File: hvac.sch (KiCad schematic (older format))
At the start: 44 parts, among them IC1 ATMEGA328P-A, J1 PROGRAMMING HEADER, J2 SERIAL PORT, J3 POWER_INPUT, M1 PINHD-1X10, SW1 SPST, SW2 SPST, SW3 SPST, U1 MIC5225, U2 MOSFET_N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

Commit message: Begin routing
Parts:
- removed D1, D5: RED, MF_LEDs:MF_LEDs-LED0603, symbol LED
- removed D2: YELLOW, MF_LEDs:MF_LEDs-LED0603, symbol LED
- removed D3: GREEN, MF_LEDs:MF_LEDs-LED0603, symbol LED
- removed D4: BLUE, MF_LEDs:MF_LEDs-LED0603, symbol LED
- removed M1: PINHD-1X10, Air_Coils_SML_NEOSID:Neosid_Air-Coil_SML_1turn_HDM0131A, symbol PINHD-1X10
- added D1, D5: RED, MF_LEDs:MF_LEDs-LED0603, symbol LED_SINGLE-0603-RED
- added D2: YELLOW, MF_LEDs:MF_LEDs-LED0603, symbol LED_SINGLE-0603
- added D3: GREEN, MF_LEDs:MF_LEDs-LED0603, symbol LED_SINGLE-0603-GREEN
- added D4: BLUE, MF_LEDs:MF_LEDs-LED0603, symbol LED_SINGLE-0603
- added JP2: PINHD-1X9, homebrew:1x9-RIGHT_ANGLE-0534260910, symbol PINHD-1X9
- BTN1: footprint (none) -> homebrew:EG2355-ND
- F1: footprint Air_Coils_SML_NEOSID:Neosid_Air-Coil_SML_1turn_HDM0131A -> homebrew:FUSE-3550-2
- J3: footprint Air_Coils_SML_NEOSID:Neosid_Air-Coil_SML_1turn_HDM0131A -> homebrew:1x2-RIGHT_ANGLE-43160-1102
- JP1: footprint Air_Coils_SML_NEOSID:Neosid_Air-Coil_SML_1turn_HDM0131A -> homebrew:1x6-RIGHT_ANGLE-43160-3106
- RV1, RV2: footprint Air_Coils_SML_NEOSID:Neosid_Air-Coil_SML_1turn_HDM0131A -> homebrew:PDB12-H4301-103BF
- SW1, SW2, SW3: footprint Air_Coils_SML_NEOSID:Neosid_Air-Coil_SML_1turn_HDM0131A -> homebrew:EG2355-ND
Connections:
- wire segments 118 -> 102
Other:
- moved on the sheet: R5, R6, R7, R8, R9
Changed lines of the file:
@@
 L RESISTOR0402 R5
 U 1 1 590EB7DD
-P 5450 6800
-F 0 "R5" H 5300 6859 50  0000 L BNN
-F 1 "2.2k" H 5300 6670 50  0000 L BNN
-F 2 "Resistors_SMD:R_0402" H 5480 6950 20  0001 C CNN
-F 3 "" H 5450 6800 60  0000 C CNN
-	1    5450 6800
+P 5450 7100
+F 0 "R5" H 5300 7159 50  0000 L BNN
+F 1 "2.2k" H 5300 6970 50  0000 L BNN
+F 2 "Resistors_SMD:R_0402" H 5480 7250 20  0001 C CNN
+F 3 "" H 5450 7100 60  0000 C CNN
+	1    5450 7100
 	0    1    1    0
 $EndComp
@@
 L RESISTOR0402 R6
 U 1 1 590EB81A
-P 5750 6800
-F 0 "R6" H 5600 6859 50  0000 L BNN
-F 1 "2.2k" H 5600 6670 50  0000 L BNN
-F 2 "Resistors_SMD:R_0402" H 5780 6950 20  0001 C CNN
-F 3 "" H 5750 6800 60  0000 C CNN
-	1    5750 6800
+P 5750 7100
+F 0 "R6" H 5600 7159 50  0000 L BNN
+F 1 "2.2k" H 5600 6970 50  0000 L BNN
+F 2 "Resistors_SMD:R_0402" H 5780 7250 20  0001 C CNN
+F 3 "" H 5750 7100 60  0000 C CNN
+	1    5750 7100
 	0    1    1    0
 $EndComp
@@
 L RESISTOR0402 R7
 U 1 1 590EB84F
-P 6050 6800
-F 0 "R7" H 5900 6859 50  0000 L BNN
-F 1 "2.2k" H 5900 6670 50  0000 L BNN
-F 2 "Resistors_SMD:R_0402" H 6080 6950 20  0001 C CNN
-F 3 "" H 6050 6800 60  0000 C CNN
-	1    6050 6800
-	0    1    1    0
-$EndComp
-$Comp
-L LED D1
-U 1 1 590EB886
-P 5450 7250
-F 0 "D1" H 5450 7350 50  0000 C CNN
-F 1 "RED" H 5450 7150 50  0000 C CNN
-F 2 "MF_LEDs:MF_LEDs-LED0603" H 5450 7250 50  0001 C CNN
-F 3 "" H 5450 7250 50  0000 C CNN
-	1    5450 7250
-	0    -1   -1   0
-$EndComp
-$Comp
-L LED D2
-U 1 1 590EB8BF
-P 5750 7250
-F 0 "D2" H 5750 7350 50  0000 C CNN
-F 1 "YELLOW" H 5750 7150 50  0000 C CNN
-F 2 "MF_LEDs:MF_LEDs-LED0603" H 5750 7250 50  0001 C CNN
-F 3 "" H 5750 7250 50  0000 C CNN
-	1    5750 7250
-	0    -1   -1   0
-$EndComp
-$Comp
-L LED D3
-U 1 1 590EB8F6
-P 6050 7250
-F 0 "D3" H 6050 7350 50  0000 C CNN
-F 1 "GREEN" H 6050 7150 50  0000 C CNN
-F 2 "MF_LEDs:MF_LEDs-LED0603" H 6050 7250 50  0001 C CNN
-F 3 "" H 6050 7250 50  0000 C CNN
-	1    6050 7250
-	0    -1   -1   0
-$EndComp
-Wire Wire Line
-	6050 7000 6050 7050
-Wire Wire Line
-	5750 7050 5750 7000
-Wire Wire Line
-	5450 7000 5450 7050
-Wire Wire Line
-	5450 7450 5450 7500
-Wire Wire Line
-	5750 7500 5750 7450
-Wire Wire Line
-	6050 7450 6050 7500
-Text GLabel 5450 6550 1    60   Input ~ 0
+P 6050 7100
+F 0 "R7" H 5900 7159 50  0000 L BNN
+F 1 "2.2k" H 5900 6970 50  0000 L BNN
+F 2 "Resistors_SMD:R_0402" H 6080 7250 20  0001 C CNN
+F 3 "" H 6050 7100 60  0000 C CNN
+	1    6050 7100
+	0    1    1    0
+$EndComp
+Text GLabel 5450 6900 1    60   Input ~ 0
 LED_R
-Wire Wire Line
-	5450 6550 5450 6600
-Wire Wire Line
-	5750 6600 5750 6550
-Wire Wire Line
-	6050 6550 6050 6600
-Text GLabel 6050 6550 1    60   Input ~ 0
+Text GLabel 6050 6900 1    60   Input ~ 0
 LED_G
-Text GLabel 5750 6550 1    60   Input ~ 0
+Text GLabel 5750 6900 1    60   Input ~ 0
 LED_Y
 Wire Notes Line
@@
 L RESISTOR0402 R8
 U 1 1 590EC9AA
-P 6350 6800
-F 0 "R8" H 6200 6859 50  0000 L BNN
-F 1 "2.2k" H 6200 6670 50  0000 L BNN
-F 2 "Resistors_SMD:R_0402" H 6380 6950 20  0001 C CNN
-F 3 "" H 6350 6800 60  0000 C CNN
-	1    6350 6800
-	0    1    1    0
-$EndComp
-$Comp
-L LED D4
-U 1 1 590EC9B0
-P 6350 7250
-F 0 "D4" H 6350 7350 50  0000 C CNN
-F 1 "BLUE" H 6350 7150 50  0000 C CNN
-F 2 "MF_LEDs:MF_LEDs-LED0603" H 6350 7250 50  0001 C CNN
-F 3 "" H 6350 7250 50  0000 C CNN
-	1    6350 7250
-	0    -1   -1   0
-$EndComp
-Wire Wire Line
-	6350 7000 6350 7050
-Wire Wire Line
-	6350 7450 6350 7500
-Wire Wire Line
-	6350 6550 6350 6600
-Text GLabel 6350 6550 1    60   Input ~ 0
+P 6350 7100
+F 0 "R8" H 6200 7159 50  0000 L BNN
+F 1 "2.2k" H 6200 6970 50  0000 L BNN
+F 2 "Resistors_SMD:R_0402" H 6380 7250 20  0001 C CNN
+F 3 "" H 6350 7100 60  0000 C CNN
+	1    6350 7100
+	0    1    1    0
+$EndComp
+Text GLabel 6350 6900 1    60   Input ~ 0
 LED_TIMER
 $Comp
@@
 F 0 "SW1" H 9500 800 50  0000 C CNN
 F 1 "SPST" H 9500 600 50  0000 C CNN
-F 2 "Air_Coils_SML_NEOSID:Neosid_Air-Coil_SML_1turn_HDM0131A" H 9500 700 50  0001 C CNN
+F 2 "homebrew:EG2355-ND" H 9500 700 50  0001 C CNN
 F 3 "" H 9500 700 50  0000 C CNN
 	1    9500 700
@@
 F 0 "SW2" H 9500 1050 50  0000 C CNN
 F 1 "SPST" H 9500 850 50  0000 C CNN
-F 2 "Air_Coils_SML_NEOSID:Neosid_Air-Coil_SML_1turn_HDM0131A" H 9500 950 50  0001 C CNN
+F 2 "homebrew:EG2355-ND" H 9500 950 50  0001 C CNN
 F 3 "" H 9500 950 50  0000 C CNN
 	1    9500 950
@@
 F 0 "SW3" H 9500 1300 50  0000 C CNN
 F 1 "SPST" H 9500 1100 50  0000 C CNN
-F 2 "Air_Coils_SML_NEOSID:Neosid_Air-Coil_SML_1turn_HDM0131A" H 9500 1200 50  0001 C CNN
+F 2 "homebrew:EG2355-ND" H 9500 1200 50  0001 C CNN
 F 3 "" H 9500 1200 50  0000 C CNN
 	1    9500 1200
@@
 F 0 "RV1" H 9350 1920 50  0000 C CNN
 F 1 "POT" H 9350 2000 50  0000 C CNN
-F 2 "Air_Coils_SML_NEOSID:Neosid_Air-Coil_SML_1turn_HDM0131A" H 9350 2000 50  0001 C CNN
+F 2 "homebrew:PDB12-H4301-103BF" H 9350 2000 50  0001 C CNN
 F 3 "" H 9350 2000 50  0000 C CNN
 	1    9350 2000
@@
 F 0 "RV2" H 9350 2470 50  0000 C CNN
 F 1 "POT" H 9350 2550 50  0000 C CNN
-F 2 "Air_Coils_SML_NEOSID:Neosid_Air-Coil_SML_1turn_HDM0131A" H 9350 2550 50  0001 C CNN
+F 2 "homebrew:PDB12-H4301-103BF" H 9350 2550 50  0001 C CNN
 F 3 "" H 9350 2550 50  0000 C CNN
 	1    9350 2550
@@
 L RESISTOR0402 R9
 U 1 1 590F35DB
-P 6650 6800
-F 0 "R9" H 6500 6859 50  0000 L BNN
-F 1 "2.2k" H 6500 6670 50  0000 L BNN
-F 2 "Resistors_SMD:R_0402" H 6680 6950 20  0001 C CNN
-F 3 "" H 6650 6800 60  0000 C CNN
-	1    6650 6800
-	0    1    1    0
-$EndComp
-$Comp
-L LED D5
-U 1 1 590F35E1
-P 6650 7250
-F 0 "D5" H 6650 7350 50  0000 C CNN
-F 1 "RED" H 6650 7150 50  0000 C CNN
-F 2 "MF_LEDs:MF_LEDs-LED0603" H 6650 7250 50  0001 C CNN
-F 3 "" H 6650 7250 50  0000 C CNN
-	1    6650 7250
-	0    -1   -1   0
-$EndComp
-Wire Wire Line
-	6650 7000 6650 7050
-Wire Wire Line
-	6650 7450 6650 7500
-Wire Wire Line
-	6650 6550 6650 6600
-Text GLabel 6650 6550 1    60   Input ~ 0
+P 6650 7100
+F 0 "R9" H 6500 7159 50  0000 L BNN
+F 1 "2.2k" H 6500 6970 50  0000 L BNN
+F 2 "Resistors_SMD:R_0402" H 6680 7250 20  0001 C CNN
+F 3 "" H 6650 7100 60  0000 C CNN
+	1    6650 7100
+	0    1    1    0
+$EndComp
+Text GLabel 6650 6900 1    60   Input ~ 0
 LED_WATER_LIMIT
 Wire Wire Line
@@
 F 0 "BTN1" H 9500 1550 50  0000 C CNN
 F 1 "SPST" H 9500 1350 50  0001 C CNN
-F 2 "" H 9500 1450 50  0001 C CNN
+F 2 "homebrew:EG2355-ND" H 9500 1450 50  0001 C CNN
 F 3 "" H 9500 1450 50  0000 C CNN
 	1    9500 1450
@@
 F 0 "J3" H 4800 6150 50  0001 C CNN
 F 1 "POWER_INPUT" H 4800 6150 50  0001 C CNN
-F 2 "Air_Coils_SML_NEOSID:Neosid_Air-Coil_SML_1turn_HDM0131A" H 4830 6300 20  0001 C CNN
+F 2 "homebrew:1x2-RIGHT_ANGLE-43160-1102" H 4830 6300 20  0001 C CNN
 F 3 "" H 4800 6150 60  0000 C CNN
 	1    4800 6150
@@
 F 0 "JP1" H 10200 5375 50  0000 L BNN
 F 1 "PINHD-1X6" H 10200 4550 50  0000 L BNN
-F 2 "Air_Coils_SML_NEOSID:Neosid_Air-Coil_SML_1turn_HDM0131A" H 10480 5100 20  0001 C CNN
+F 2 "homebrew:1x6-RIGHT_ANGLE-43160-3106" H 10480 5100 20  0001 C CNN
 F 3 "" H 10450 4950 60  0000 C CNN
 	1    10450 4950
@@
 F 0 "F1" H 3800 6150 50  0000 L BNN
 F 1 "POWER_FUSE" H 4400 6150 50  0000 L BNN
-F 2 "Air_Coils_SML_NEOSID:Neosid_Air-Coil_SML_1turn_HDM0131A" H 4230 6200 20  0001 C CNN
+F 2 "homebrew:FUSE-3550-2" H 4230 6200 20  0001 C CNN
 F 3 "" H 4200 6050 60  0000 C CNN
 	1    4200 6050
@@
 Text Notes 350  6400 0    60   ~ 0
 TODO: Verify programming port
-$Comp
-L PINHD-1X10 M1
-U 1 1 5910F906
-P 10450 3650
-F 0 "M1" H 10200 4175 50  0000 L BNN
-F 1 "PINHD-1X10" H 10200 2950 50  0000 L BNN
-F 2 "Air_Coils_SML_NEOSID:Neosid_Air-Coil_SML_1turn_HDM0131A" H 10480 3800 20  0001 C CNN
-F 3 "" H 10450 3650 60  0000 C CNN
-	1    10450 3650
-	1    0    0    -1
-$EndComp
 Wire Wire Line
 	9150 3200 9150 3650
@@
 	10350 3950 9250 3950
 Connection ~ 9250 3950
-Wire Wire Line
-	9250 4150 10350 4150
 Connection ~ 9250 4150
 Wire Wire Line
@@
 	800  1600 800  1800
 Wire Wire Line
-	800  1300 800  1150
+	800  1150 800  1300
 Wire Wire Line
 	1950 1500 1950 1800
@@
 Wire Wire Line
 	1200 1500 1950 1500
+$Comp
+L PINHD-1X9 JP2
+U 1 1 591172FD
+P 10450 3650
+F 0 "JP2" H 10200 4175 50  0000 L BNN
+F 1 "PINHD-1X9" H 10200 3050 50  0000 L BNN
+F 2 "homebrew:1x9-RIGHT_ANGLE-0534260910" H 10480 3800 20  0001 C CNN
+F 3 "" H 10450 3650 60  0000 C CNN
+	1    10450 3650
+	1    0    0    -1
+$EndComp
+$Comp
+L LED_SINGLE-0603-RED D1
+U 1 1 59119842
+P 5450 7400
+F 0 "D1" H 5350 7300 45  0000 L BNN
+F 1 "RED" H 5350 7200 45  0000 L BNN
+F 2 "MF_LEDs:MF_LEDs-LED0603" H 5480 7550 20  0001 C CNN
+F 3 "" H 5450 7400 60  0001 C CNN
+	1    5450 7400
+	0    1    1    0
+$EndComp
+$Comp
+L LED_SINGLE-0603 D2
+U 1 1 59119B10
+P 5750 7400
+F 0 "D2" H 5650 7300 45  0000 L BNN
+F 1 "YELLOW" H 5650 7200 45  0000 L BNN
+F 2 "MF_LEDs:MF_LEDs-LED0603" H 5780 7550 20  0001 C CNN
+F 3 "" H 5750 7400 60  0001 C CNN
+	1    5750 7400
+	0    1    1    0
+$EndComp
+$Comp
+L LED_SINGLE-0603-GREEN D3
+U 1 1 59119E03
+P 6050 7400
+F 0 "D3" H 5950 7300 45  0000 L BNN
+F 1 "GREEN" H 5950 7200 45  0000 L BNN
+F 2 "MF_LEDs:MF_LEDs-LED0603" H 6080 7550 20  0001 C CNN
+F 3 "" H 6050 7400 60  0001 C CNN
+	1    6050 7400
+	0    1    1    0
+$EndComp
+$Comp
+L LED_SINGLE-0603 D4
+U 1 1 5911A03A
+P 6350 7400
+F 0 "D4" H 6250 7300 45  0000 L BNN
+F 1 "BLUE" H 6250 7200 45  0000 L BNN
+F 2 "MF_LEDs:MF_LEDs-LED0603" H 6380 7550 20  0001 C CNN
+F 3 "" H 6350 7400 60  0001 C CNN
+	1    6350 7400
+	0    1    1    0
+$EndComp
+$Comp
+L LED_SINGLE-0603-RED D5
+U 1 1 5911A388
+P 6650 7400
+F 0 "D5" H 6550 7300 45  0000 L BNN
+F 1 "RED" H 6550 7200 45  0000 L BNN
+F 2 "MF_LEDs:MF_LEDs-LED0603" H 6680 7550 20  0001 C CNN
+F 3 "" H 6650 7400 60  0001 C CNN
+	1    6650 7400
+	0    1    1    0
+$EndComp
 $EndSCHEMATC

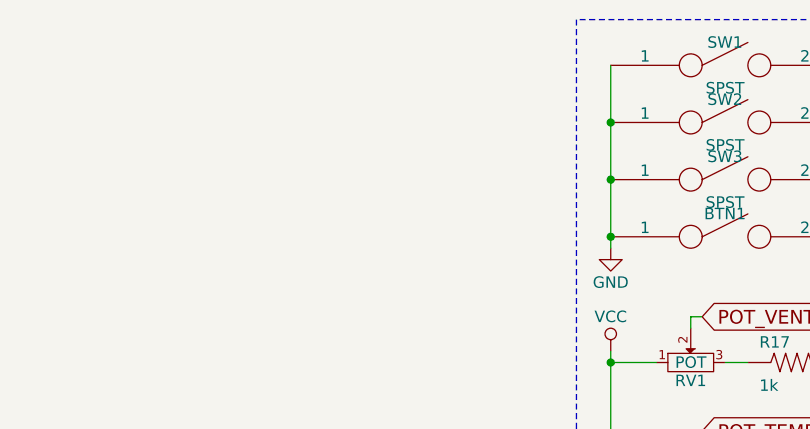
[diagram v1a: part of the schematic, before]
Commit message: Create hole footprint and route a few small things
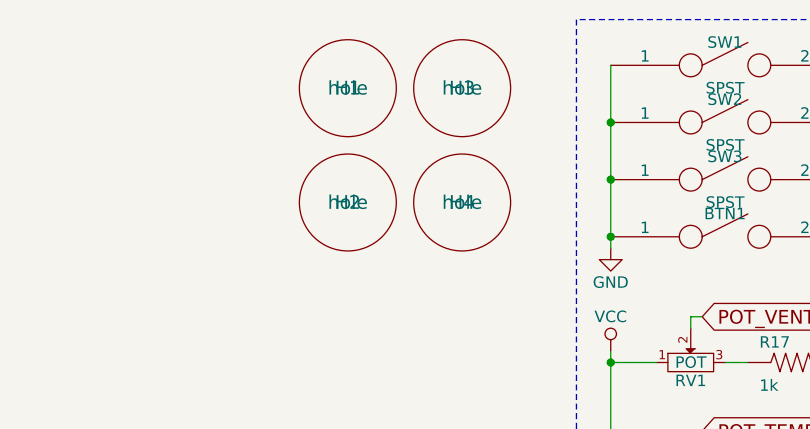
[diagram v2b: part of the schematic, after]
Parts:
- added H1, H2, H3, H4: hole, symbol hole
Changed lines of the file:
@@
 $EndComp
 $Comp
-L GND #PWR01
+L GND #PWR14
 U 1 1 590E6F18
 P 3900 6550
-F 0 "#PWR01" H 3900 6300 50  0001 C CNN
+F 0 "#PWR14" H 3900 6300 50  0001 C CNN
 F 1 "GND" H 3900 6400 50  0000 C CNN
 F 2 "" H 3900 6550 50  0000 C CNN
@@
 $EndComp
 $Comp
-L GND #PWR02
+L GND #PWR17
 U 1 1 590E705E
 P 4900 6750
-F 0 "#PWR02" H 4900 6500 50  0001 C CNN
+F 0 "#PWR17" H 4900 6500 50  0001 C CNN
 F 1 "GND" H 4900 6600 50  0000 C CNN
 F 2 "" H 4900 6750 50  0000 C CNN
@@
 $EndComp
 $Comp
-L GND #PWR03
+L GND #PWR12
 U 1 1 590E7076
 P 3650 7150
-F 0 "#PWR03" H 3650 6900 50  0001 C CNN
+F 0 "#PWR12" H 3650 6900 50  0001 C CNN
 F 1 "GND" H 3650 7000 50  0000 C CNN
 F 2 "" H 3650 7150 50  0000 C CNN
@@
 $EndComp
 $Comp
-L VCC #PWR04
+L VCC #PWR15
 U 1 1 590E72A3
 P 3900 7600
-F 0 "#PWR04" H 3900 7450 50  0001 C CNN
+F 0 "#PWR15" H 3900 7450 50  0001 C CNN
 F 1 "VCC" H 3900 7750 50  0000 C CNN
 F 2 "" H 3900 7600 50  0000 C CNN
@@
 $EndComp
 $Comp
-L VCC #PWR05
+L VCC #PWR18
 U 1 1 590E73E6
 P 4900 7250
-F 0 "#PWR05" H 4900 7100 50  0001 C CNN
+F 0 "#PWR18" H 4900 7100 50  0001 C CNN
 F 1 "VCC" H 4900 7400 50  0000 C CNN
 F 2 "" H 4900 7250 50  0000 C CNN
@@
 $EndComp
 $Comp
-L +BATT #PWR06
+L +BATT #PWR11
 U 1 1 590E74A1
 P 3600 6950
-F 0 "#PWR06" H 3600 6800 50  0001 C CNN
+F 0 "#PWR11" H 3600 6800 50  0001 C CNN
 F 1 "+BATT" H 3600 7090 50  0000 C CNN
 F 2 "" H 3600 6950 50  0000 C CNN
@@
 $EndComp
 $Comp
-L VCC #PWR07
+L VCC #PWR6
 U 1 1 590E75CA
 P 1200 1500
-F 0 "#PWR07" H 1200 1350 50  0001 C CNN
+F 0 "#PWR6" H 1200 1350 50  0001 C CNN
 F 1 "VCC" H 1200 1650 50  0000 C CNN
 F 2 "" H 1200 1500 50  0000 C CNN
@@
 $EndComp
 $Comp
-L GND #PWR08
+L GND #PWR4
 U 1 1 590E76C4
 P 800 1800
-F 0 "#PWR08" H 800 1550 50  0001 C CNN
+F 0 "#PWR4" H 800 1550 50  0001 C CNN
 F 1 "GND" H 800 1650 50  0000 C CNN
 F 2 "" H 800 1800 50  0000 C CNN
@@
 $EndComp
 $Comp
-L GND #PWR09
+L GND #PWR8
 U 1 1 590E77C7
 P 1850 3600
-F 0 "#PWR09" H 1850 3350 50  0001 C CNN
+F 0 "#PWR8" H 1850 3350 50  0001 C CNN
 F 1 "GND" H 1850 3450 50  0000 C CNN
 F 2 "" H 1850 3600 50  0000 C CNN
@@
 RST
 $Comp
-L GND #PWR010
+L GND #PWR5
 U 1 1 590E81EE
 P 1050 6550
-F 0 "#PWR010" H 1050 6300 50  0001 C CNN
+F 0 "#PWR5" H 1050 6300 50  0001 C CNN
 F 1 "GND" H 1050 6400 50  0000 C CNN
 F 2 "" H 1050 6550 50  0000 C CNN
@@
 TXO
 $Comp
-L VCC #PWR011
+L VCC #PWR20
 U 1 1 590E887E
 P 5500 2650
-F 0 "#PWR011" H 5500 2500 50  0001 C CNN
+F 0 "#PWR20" H 5500 2500 50  0001 C CNN
 F 1 "VCC" H 5500 2800 50  0000 C CNN
 F 2 "" H 5500 2650 50  0000 C CNN
@@
 	4900 6800 4900 6750
 $Comp
-L GND #PWR012
+L GND #PWR19
 U 1 1 590EB74E
 P 5450 7500
-F 0 "#PWR012" H 5450 7250 50  0001 C CNN
+F 0 "#PWR19" H 5450 7250 50  0001 C CNN
 F 1 "GND" H 5450 7350 50  0000 C CNN
 F 2 "" H 5450 7500 50  0000 C CNN
@@
 $EndComp
 $Comp
-L GND #PWR013
+L GND #PWR21
 U 1 1 590EB774
 P 5750 7500
-F 0 "#PWR013" H 5750 7250 50  0001 C CNN
+F 0 "#PWR21" H 5750 7250 50  0001 C CNN
 F 1 "GND" H 5750 7350 50  0000 C CNN
 F 2 "" H 5750 7500 50  0000 C CNN
@@
 $EndComp
 $Comp
-L GND #PWR014
+L GND #PWR22
 U 1 1 590EB798
 P 6050 7500
-F 0 "#PWR014" H 6050 7250 50  0001 C CNN
+F 0 "#PWR22" H 6050 7250 50  0001 C CNN
 F 1 "GND" H 6050 7350 50  0000 C CNN
 F 2 "" H 6050 7500 50  0000 C CNN
@@
 Power Supply
 $Comp
-L GND #PWR015
+L GND #PWR23
 U 1 1 590EC9A4
 P 6350 7500
-F 0 "#PWR015" H 6350 7250 50  0001 C CNN
+F 0 "#PWR23" H 6350 7250 50  0001 C CNN
 F 1 "GND" H 6350 7350 50  0000 C CNN
 F 2 "" H 6350 7500 50  0000 C CNN
@@
 $EndComp
 $Comp
-L GND #PWR016
+L GND #PWR28
 U 1 1 590EF13D
 P 9000 1500
-F 0 "#PWR016" H 9000 1250 50  0001 C CNN
+F 0 "#PWR28" H 9000 1250 50  0001 C CNN
 F 1 "GND" H 9000 1350 50  0000 C CNN
 F 2 "" H 9000 1500 50  0000 C CNN
@@
 $EndComp
 $Comp
-L VCC #PWR017
+L VCC #PWR29
 U 1 1 590EFAF0
 P 9000 1950
-F 0 "#PWR017" H 9000 1800 50  0001 C CNN
+F 0 "#PWR29" H 9000 1800 50  0001 C CNN
 F 1 "VCC" H 9000 2100 50  0000 C CNN
 F 2 "" H 9000 1950 50  0000 C CNN
@@
 	9500 2000 9600 2000
 $Comp
-L GND #PWR018
+L GND #PWR33
 U 1 1 590F0610
 P 10350 2600
-F 0 "#PWR018" H 10350 2350 50  0001 C CNN
+F 0 "#PWR33" H 10350 2350 50  0001 C CNN
 F 1 "GND" H 10350 2450 50  0000 C CNN
 F 2 "" H 10350 2600 50  0000 C CNN
@@
 BTN_TIMER
 $Comp
-L GND #PWR019
+L GND #PWR24
 U 1 1 590F35D5
 P 6650 7500
-F 0 "#PWR019" H 6650 7250 50  0001 C CNN
+F 0 "#PWR24" H 6650 7250 50  0001 C CNN
 F 1 "GND" H 6650 7350 50  0000 C CNN
 F 2 "" H 6650 7500 50  0000 C CNN
@@
 SW_VENT_OVERRIDE
 $Comp
-L GND #PWR020
+L GND #PWR2
 U 1 1 590F5B7A
 P 750 7500
-F 0 "#PWR020" H 750 7250 50  0001 C CNN
+F 0 "#PWR2" H 750 7250 50  0001 C CNN
 F 1 "GND" H 750 7350 50  0000 C CNN
 F 2 "" H 750 7500 50  0000 C CNN
@@
 	750  7500 900  7500
 $Comp
-L VCC #PWR021
+L VCC #PWR1
 U 1 1 590F5CC0
 P 750 7300
-F 0 "#PWR021" H 750 7150 50  0001 C CNN
+F 0 "#PWR1" H 750 7150 50  0001 C CNN
 F 1 "VCC" H 750 7450 50  0000 C CNN
 F 2 "" H 750 7300 50  0000 C CNN
@@
 TEMP_OUTSIDE
 $Comp
-L VCC #PWR022
+L VCC #PWR30
 U 1 1 590F74AC
 P 9150 3200
-F 0 "#PWR022" H 9150 3050 50  0001 C CNN
+F 0 "#PWR30" H 9150 3050 50  0001 C CNN
 F 1 "VCC" H 9150 3350 50  0000 C CNN
 F 2 "" H 9150 3200 50  0000 C CNN
@@
 $EndComp
 $Comp
-L GND #PWR023
+L GND #PWR16
 U 1 1 590FA0A9
 P 4600 6150
-F 0 "#PWR023" H 4600 5900 50  0001 C CNN
+F 0 "#PWR16" H 4600 5900 50  0001 C CNN
 F 1 "GND" H 4600 6000 50  0000 C CNN
 F 2 "" H 4600 6150 50  0000 C CNN
@@
 $EndComp
 $Comp
-L +BATT #PWR024
+L +BATT #PWR13
 U 1 1 590FA14E
 P 3800 6050
-F 0 "#PWR024" H 3800 5900 50  0001 C CNN
+F 0 "#PWR13" H 3800 5900 50  0001 C CNN
 F 1 "+BATT" H 3800 6190 50  0000 C CNN
 F 2 "" H 3800 6050 50  0000 C CNN
@@
 Power Connector
 $Comp
-L GND #PWR025
+L GND #PWR10
 U 1 1 590FBCD1
 P 3100 7550
-F 0 "#PWR025" H 3100 7300 50  0001 C CNN
+F 0 "#PWR10" H 3100 7300 50  0001 C CNN
 F 1 "GND" H 3100 7400 50  0000 C CNN
 F 2 "" H 3100 7550 50  0000 C CNN
@@
 $EndComp
 $Comp
-L +BATT #PWR026
+L +BATT #PWR9
 U 1 1 590FC073
 P 3100 6450
-F 0 "#PWR026" H 3100 6300 50  0001 C CNN
+F 0 "#PWR9" H 3100 6300 50  0001 C CNN
 F 1 "+BATT" H 3100 6590 50  0000 C CNN
 F 2 "" H 3100 6450 50  0000 C CNN
@@
 Programming Ports
 $Comp
-L GND #PWR027
+L GND #PWR31
 U 1 1 590FE215
 P 9250 4200
-F 0 "#PWR027" H 9250 3950 50  0001 C CNN
+F 0 "#PWR31" H 9250 3950 50  0001 C CNN
 F 1 "GND" H 9250 4050 50  0000 C CNN
 F 2 "" H 9250 4200 50  0000 C CNN
@@
 $EndComp
 $Comp
-L GND #PWR028
+L GND #PWR26
 U 1 1 59102A56
 P 8800 5200
-F 0 "#PWR028" H 8800 4950 50  0001 C CNN
+F 0 "#PWR26" H 8800 4950 50  0001 C CNN
 F 1 "GND" H 8800 5050 50  0000 C CNN
 F 2 "" H 8800 5200 50  0000 C CNN
@@
 $EndComp
 $Comp
-L +BATT #PWR029
+L +BATT #PWR32
 U 1 1 59102C3A
 P 9250 4550
-F 0 "#PWR029" H 9250 4400 50  0001 C CNN
+F 0 "#PWR32" H 9250 4400 50  0001 C CNN
 F 1 "+BATT" H 9250 4690 50  0000 C CNN
 F 2 "" H 9250 4550 50  0000 C CNN
@@
 $EndComp
 $Comp
-L GND #PWR030
+L GND #PWR27
 U 1 1 591065E6
 P 8800 6250
-F 0 "#PWR030" H 8800 6000 50  0001 C CNN
+F 0 "#PWR27" H 8800 6000 50  0001 C CNN
 F 1 "GND" H 8800 6100 50  0000 C CNN
 F 2 "" H 8800 6250 50  0000 C CNN
@@
 $EndComp
 $Comp
-L GND #PWR031
+L GND #PWR25
 U 1 1 591067B3
 P 8800 4150
-F 0 "#PWR031" H 8800 3900 50  0001 C CNN
+F 0 "#PWR25" H 8800 3900 50  0001 C CNN
 F 1 "GND" H 8800 4000 50  0000 C CNN
 F 2 "" H 8800 4150 50  0000 C CNN
@@
 $EndComp
 $Comp
-L VCC #PWR032
+L VCC #PWR3
 U 1 1 59112013
 P 800 1150
-F 0 "#PWR032" H 800 1000 50  0001 C CNN
+F 0 "#PWR3" H 800 1000 50  0001 C CNN
 F 1 "VCC" H 800 1300 50  0000 C CNN
 F 2 "" H 800 1150 50  0000 C CNN
@@
 $EndComp
 $Comp
-L GND #PWR033
+L GND #PWR7
 U 1 1 59112187
 P 1200 1800
-F 0 "#PWR033" H 1200 1550 50  0001 C CNN
+F 0 "#PWR7" H 1200 1550 50  0001 C CNN
 F 1 "GND" H 1200 1650 50  0000 C CNN
 F 2 "" H 1200 1800 50  0000 C CNN
@@
 	0    1    1    0
 $EndComp
+$Comp
+L hole H3
+U 1 1 5938C6A6
+P 8350 800
+F 0 "H3" H 8350 800 60  0000 C CNN
+F 1 "hole" H 8350 800 60  0000 C CNN
+F 2 "" H 8350 800 60  0000 C CNN
+F 3 "" H 8350 800 60  0000 C CNN
+	1    8350 800
+	1    0    0    -1
+$EndComp
+$Comp
+L hole H4
+U 1 1 5938C761
+P 8350 1300
+F 0 "H4" H 8350 1300 60  0000 C CNN
+F 1 "hole" H 8350 1300 60  0000 C CNN
+F 2 "" H 8350 1300 60  0000 C CNN
+F 3 "" H 8350 1300 60  0000 C CNN
+	1    8350 1300
+	1    0    0    -1
+$EndComp
+$Comp
+L hole H1
+U 1 1 5938C7F4
+P 7850 800
+F 0 "H1" H 7850 800 60  0000 C CNN
+F 1 "hole" H 7850 800 60  0000 C CNN
+F 2 "" H 7850 800 60  0000 C CNN
+F 3 "" H 7850 800 60  0000 C CNN
+	1    7850 800
+	1    0    0    -1
+$EndComp
+$Comp
+L hole H2
+U 1 1 5938C86D
+P 7850 1300
+F 0 "H2" H 7850 1300 60  0000 C CNN
+F 1 "hole" H 7850 1300 60  0000 C CNN
+F 2 "" H 7850 1300 60  0000 C CNN
+F 3 "" H 7850 1300 60  0000 C CNN
+	1    7850 1300
+	1    0    0    -1
+$EndComp
 $EndSCHEMATC
